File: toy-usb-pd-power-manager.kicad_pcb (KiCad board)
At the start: 4 copper layers, 26.2 x 52.1 mm, 162 parts, among them J1 USB_C_2_0, J2 PINS_LHS, J3 PINS_RHS, Q1 Si7223DN, Q2 Si7224DN, Q3 Si7224DN, Q4 Si7224DN, Q5 Si7223DN, Q6 BSS138PS, Q7 BSS138PS, Q8 BSS138PS, U1 HUSB238_002DD, U2 BQ25672, U3 MAX17205G, U4 TPS63070, U5 TPS7A2601DRVR

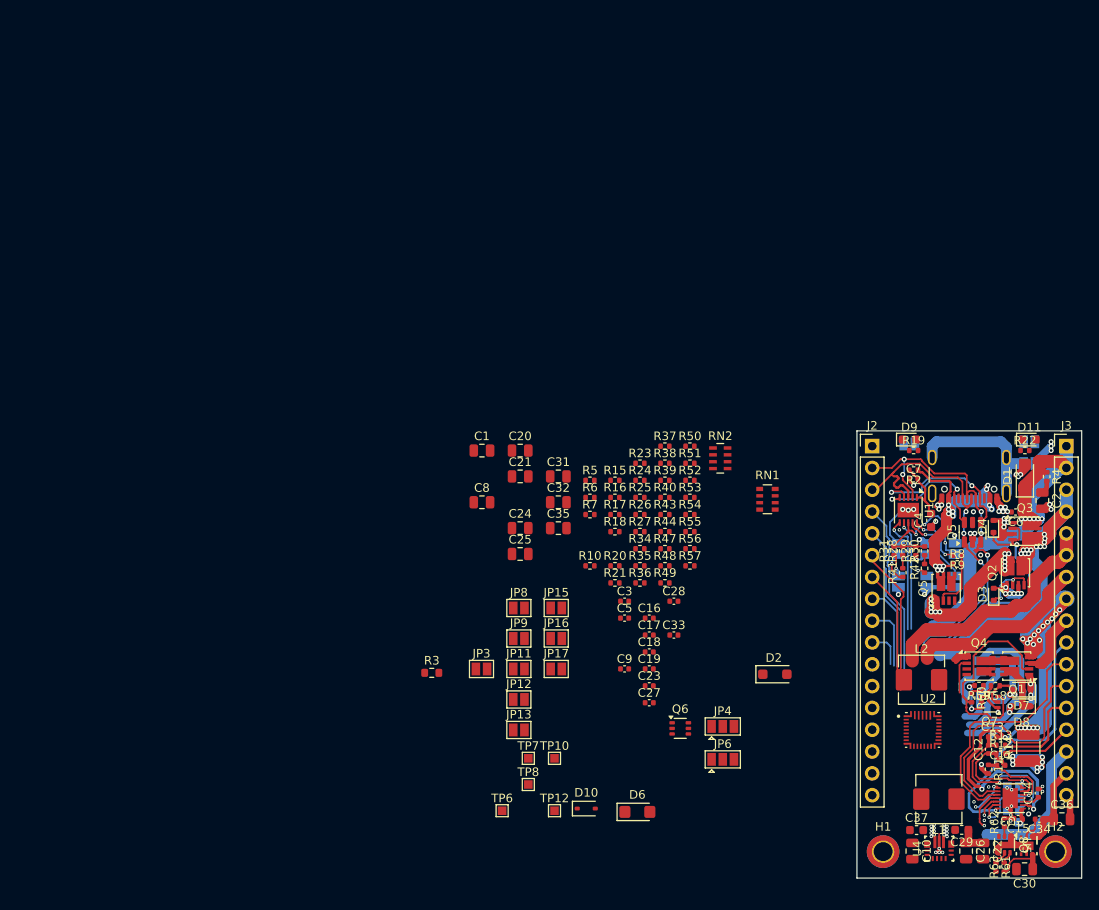
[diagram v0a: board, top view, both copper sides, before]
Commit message: refactor(pcb): improve positioning of ICs on the board
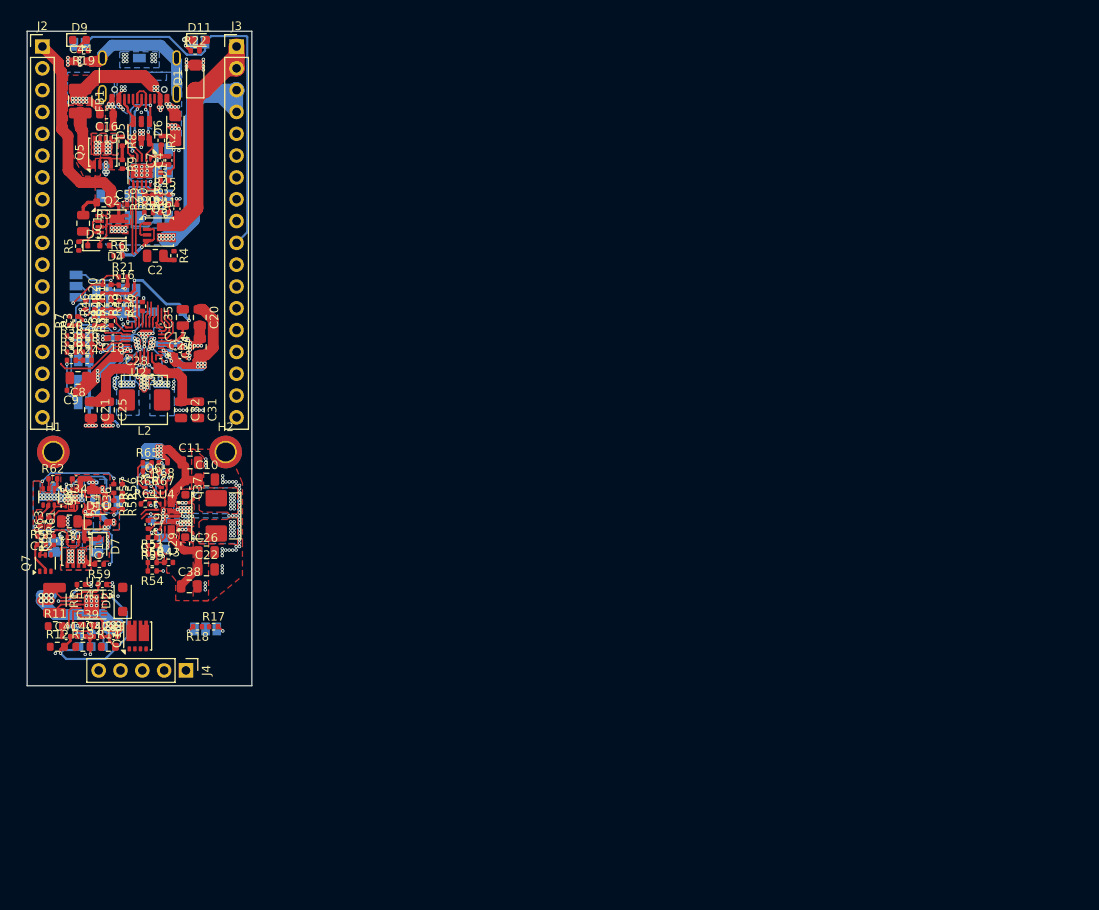
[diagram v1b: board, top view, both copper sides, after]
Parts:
- removed D8: 1N5819WS, Diode_SMD:D_SOD-323
- removed Q4: Si7224DN, Package_SO:Vishay_PowerPAK_1212-8_Dual
- removed RN1: 10M, Resistor_SMD:R_Array_Convex_4x0603
- removed RN2: 1M, Resistor_SMD:R_Array_Concave_4x0603
- removed TP1, TP2, TP3, TP4, TP5: TestPoint, TestPoint:TestPoint_Pad_1.0x1.0mm
- added C38: 47u, Capacitor_SMD:C_0805_2012Metric, F.Cu at (125.5, 119.7)
- added C39: 100n, Capacitor_SMD:C_0402_1005Metric, F.Cu at (113.6, 124.1)
- added C40: 10n, Capacitor_SMD:C_0402_1005Metric, F.Cu at (113.0, 125.5)
- added C41: 10n, Capacitor_SMD:C_0402_1005Metric, F.Cu at (111.1, 125.5)
- added C42: 10n, Capacitor_SMD:C_0402_1005Metric, F.Cu at (114.8, 125.5)
- added C43: 10n, Capacitor_SMD:C_0402_1005Metric, F.Cu at (116.6, 125.5)
- added C44: DNP, Capacitor_SMD:C_0603_1608Metric, F.Cu at (112.8, 58.6)
- added FB1: 8A, Inductor_SMD:L_1210_3225Metric, F.Cu at (112.8, 63.2)
- added J4: PINS_RHS, Connector_PinHeader_2.54mm:PinHeader_1x05_P2.54mm_Vertical, F.Cu at (125.1, 129.5)
- added JP10: BAT_ILIM_2A, Jumper:SolderJumper-2_P1.3mm_Open_Pad1.0x1.5mm, B.Cu at (115.3, 85.2)
- added JP14: BAT_PACK_4S, Jumper:SolderJumper-2_P1.3mm_Open_Pad1.0x1.5mm, B.Cu at (113.2, 98.3)
- added JP24: USB_ISET_2A, Jumper:SolderJumper-2_P1.3mm_Open_Pad1.0x1.5mm, B.Cu at (122.4, 68.9)
- added Q10: DMC3025LDV, mixlib-generic-son:Diodes_PowerDI3333-8_UXC_3.3x3.3mm_P0.65mm, F.Cu at (119.5, 125.5)
- added R1: 0.1, Resistor_SMD:R_1210_3225Metric, F.Cu at (109.8, 121.3)
- added R32: 10K, Resistor_SMD:R_0402_1005Metric, F.Cu at (122.6, 72.4)
- added R33: 1M, Resistor_SMD:R_0402_1005Metric, F.Cu at (115.4, 86.9)
- added R45: 510, Resistor_SMD:R_0402_1005Metric, F.Cu at (122.6, 71.5)
- added R46: 68K, Resistor_SMD:R_0402_1005Metric, F.Cu at (114.5, 86.9)
- added R64: 10M, Resistor_SMD:R_0402_1005Metric, F.Cu at (120.3, 110.1)
- added R65: 10M, Resistor_SMD:R_0402_1005Metric, F.Cu at (120.6, 105.3)
- added R66: 10M, Resistor_SMD:R_0402_1005Metric, F.Cu at (120.6, 106.3)
- added R67: 10M, Resistor_SMD:R_0402_1005Metric, F.Cu at (122.4, 106.3)
- added R68: 10M, Resistor_SMD:R_0402_1005Metric, F.Cu at (122.4, 105.3)
- added TP13: TestPoint, TestPoint:TestPoint_Pad_1.0x1.0mm, B.Cu at (114.1, 125.3)
- added TP14: TestPoint, TestPoint:TestPoint_Pad_1.0x1.0mm, B.Cu at (112.6, 125.3)
- added TP15: TestPoint, TestPoint:TestPoint_Pad_1.0x1.0mm, B.Cu at (115.5, 126.7)
- C11: value 1n -> 22u; footprint Capacitor_SMD:C_0402_1005Metric -> Capacitor_SMD:C_0805_2012Metric
- C12: value 1n -> 100n
- C13: value 1n -> 1u
- C14: value 470n -> 1u
- C15: value 470n -> 2.2u; footprint Capacitor_SMD:C_0402_1005Metric -> Capacitor_SMD:C_0603_1608Metric
- C16: value 100n -> 2.2u; footprint Capacitor_SMD:C_0402_1005Metric -> Capacitor_SMD:C_0603_1608Metric
- C4: value 2.2u -> 1u; footprint Capacitor_SMD:C_0603_1608Metric -> Capacitor_SMD:C_0402_1005Metric
- D3, D4: value Zener_16V -> 16V
- J2, J3: footprint Connector_PinHeader_2.54mm:PinHeader_1x17_P2.54mm_Vertical -> Connector_PinHeader_2.54mm:PinHeader_1x18_P2.54mm_Vertical
- JP11, JP12, JP13, JP15, JP16, JP17, JP3, JP4, JP6, JP8, JP9, TP10, TP12, TP6, TP7, TP8: moved to B.Cu
- R11, R12, R13: footprint Resistor_SMD:R_0402_1005Metric -> Resistor_SMD:R_0603_1608Metric
- R14: value 0.01 -> 100; footprint Resistor_SMD:R_1210_3225Metric -> Resistor_SMD:R_0603_1608Metric
- R63: value 1M -> 10M
- U3: value MAX17205G -> MAX172x5G
- moved C15 133.2 mm to (115.8, 66.2)
- moved C34 118.9 mm to (112.3, 107.2)
- moved C36 118.9 mm to (114.2, 109.5), turned to -90 degrees
- moved Q8 118.4 mm to (109.1, 109.3)
- moved C30 118.3 mm to (111.5, 112.1)
- moved U5 118.3 mm to (111.8, 109.4)
- moved R61 118.3 mm to (108.2, 112.2)
- moved R63 118.3 mm to (109.1, 112.2)
- moved R62 117.8 mm to (109.6, 107.2), turned to 0 degrees
- moved JP25 114.1 mm to (119.7, 57.6), turned to -90 degrees
- moved C14 114.1 mm to (112.9, 119.5), turned to 180 degrees
- moved C12 113.0 mm to (108.3, 113.9), turned to 180 degrees
- moved Q2 112.8 mm to (116.5, 77.5), turned to 0 degrees
- moved D3 112.4 mm to (114.3, 80.0), turned to 0 degrees
- moved R58 112.3 mm to (108.3, 114.8), turned to 0 degrees
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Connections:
- net /BC_SW_SW2 renamed /BC_SW_BTST2
- net Net-(Q6A-D) renamed /VSW_PS_EN_D
- net Net-(Q6B-D) renamed /VSW_EN_D
- C11 pad 1: /FG_VIN -> /VSW_VIN
- C11 pad 2: /FG_CELL2_TP -> GND
- C12 pad 1: /FG_CELL2_TP -> /VLDO_VIN
- C12 pad 2: /FG_CELL1_TP -> GND
- C13 pad 1: /FG_CELL1_TP -> GND
- C13 pad 2: /VBATN -> /FG_REG3
- C14 pad 1: /FG_REG2 -> GND
- C14 pad 2: GND -> /FG_REG2
- C15 pad 1: /FG_REG3 -> GND
- C15 pad 2: GND -> /USB_VBUS
- C16 pad 1: /FG_VIN -> GND
- C16 pad 2: GND -> /USB_VBUS_PRE
- C20 pad 1: /VIN -> /BC_VIN
- C24 pad 1: /VIN -> /BC_VIN
- C27 pad 1: /VIN -> /BC_VIN
- D6 pad 1: /USB_VBUS -> /USB_VBUS_PRE
- J1 pad A4: /USB_VBUS -> /USB_VBUS_PRE
- J1 pad A9: /USB_VBUS -> /USB_VBUS_PRE
- J1 pad B4: /USB_VBUS -> /USB_VBUS_PRE
- J1 pad B9: /USB_VBUS -> /USB_VBUS_PRE
- J2 pad 11: /VSW_VIN -> /FG_TS_VCC
- J2 pad 12: /VLDO_VIN1 -> /FG_TS1
- J2 pad 13: /VLDO_VIN2 -> /FG_TS2
- J2 pad 14: /~{INT} -> GND
- J2 pad 15: /SCL -> /~{INT}
- J2 pad 16: /SDA -> /SCL
- J2 pad 17: GND -> /SDA
- J3 pad 10: /FG_TS_VCC -> /VBATP
- J3 pad 11: /FG_TS2 -> /BC_REGN
- J3 pad 12: /FG_TS1 -> /BC_TS
- J3 pad 13: /FG_CELL1 -> /VSW_VIN
- J3 pad 14: /FG_CELL2 -> /VLDO_VIN1
- J3 pad 15: /VSW -> /VLDO_VIN2
- J3 pad 16: /VLDO -> /VSW
- J3 pad 17: GND -> /VLDO
- J3 pad 8: /VBATN -> /VSYS
- J3 pad 9: /VBATP -> /VBATN
- JP6 pad 2: /FG_TS1 -> /BC_TS
- Q1 pad 3: /VBATP -> /VLDO_VIN2
- Q1 pad 4: /VBATN -> /VLDO_VIN2_EN_S
- Q1 pad 5: /VBATP_RPP -> /VLDO_VIN2_EN_G
- Q1 pad 6: /VLDO_VIN2_S -> /VLDO_VIN2_EN_G
- Q5 pad 1: /VBUS -> /USB_VBUS
- Q5 pad 2: Net-(Q5A-G) -> /USB_VBUS_G
- Q5 pad 3: unconnected-(Q5B-D-Pad3) -> /VBUS
- Q5 pad 4: unconnected-(Q5B-G-Pad4) -> /USB_VBUS_G
- Q5 pad 5: unconnected-(Q5B-S-Pad5) -> /USB_VBUS_D
- Q5 pad 6: /USB_VBUS -> /USB_VBUS_D
- R11 pad 1: /FG_VIN -> /BC_VBAT
- R11 pad 2: /BC_VBAT -> /FG_VCC
- R12 pad 1: /FG_CELL2_TP -> /FG_CELLX
- R12 pad 2: /FG_CELL2 -> /FG_CELLX_IN
- R13 pad 1: /FG_CELL1_TP -> /FG_CELL2
- R13 pad 2: /FG_CELL1 -> /FG_CELL2_IN
- R14 pad 1: GND -> /FG_CELL1
- R14 pad 2: /VBATN -> /FG_CELL1_IN
- R2 pad 1: /USB_VBUS -> /USB_VBUS_PRE
- R59 pad 1: /VLDO_VIN2_S -> /VLDO_VIN2
- R60 pad 1: /VLDO_VIN2_S -> /VLDO_VIN2_EN_G
- R8 pad 1: /USB_VBUS -> /USB_VBUS_D
- R8 pad 2: Net-(Q5A-G) -> /USB_VBUS_G
- R9 pad 1: Net-(Q5A-G) -> /USB_VBUS_G
- TP11 pad 1: /FG_REG3 -> /FG_CELL2_IN
- TP9 pad 1: GND -> /FG_CELLX_IN
- U2 pad 16: /FG_TS1 -> /BC_TS
- U3 pad 13: /FG_CELLX_TP -> /FG_CELLX_IN
- U3 pad 5: /FG_VIN -> /FG_VCC
- U3 pad 6: /FG_CELL2_TP -> /FG_CELL2_IN
- U3 pad 7: /FG_CELL1_TP -> /FG_CELL1_IN
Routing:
- net GND: track 89.4 -> 173.0 mm, vias 56 -> 256
- net /BC_REGN: track 0.00 -> 68.9 mm, vias 0 -> 2
- net /VBATN: track 92.6 -> 27.9 mm, vias 21 -> 12
- net /USB_VBUS: track 44.0 -> 6.44 mm, vias 14 -> 0
- net /BC_VBAT: track 5.38 -> 40.9 mm, vias 1 -> 8
- net /BC_SW_L2: track 0.00 -> 32.7 mm, vias 0 -> 21
- net /USB_D+: track 46.1 -> 14.5 mm, vias 5 -> 2
- net /USB_D-: track 44.5 -> 14.0 mm, vias 3 -> 2
- net /FG_TS_VCC: track 29.7 -> 0.00 mm, vias 1 -> 0
- net /BC_SW_L1: track 0.00 -> 29.7 mm, vias 0 -> 21
- net /FG_TS1: track 28.8 -> 0.00 mm
- net /FG_TS2: track 28.5 -> 0.00 mm
- net /USB_VBUS_PRE: track 0.00 -> 26.4 mm, vias 0 -> 30
- net /BC_VIN: track 43.9 -> 67.8 mm, vias 12 -> 32
- net /VSW_VIN: track 0.00 -> 23.0 mm, vias 0 -> 8
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- added copper zone on B.Cu, net /BC_SW_L1
- added copper zone on B.Cu, net /BC_SW_L2
- added copper zone on B.Cu, net /BC_VIN
- added copper zone on F.Cu, net /USB_VBUS
- added copper zone on B.Cu, net /USB_VBUS_D
- added copper zone on F.Cu, net /USB_VBUS_D
- added copper zone on B.Cu, net /USB_VBUS_PRE
- added copper zone on F.Cu, net /USB_VBUS_PRE
- added copper zone on F.Cu, net /VBUS
- added copper zone on B.Cu, net /VLDO
- added copper zone on F.Cu, net /VLDO
- added copper zone on F.Cu, net /VLDO_VIN
- added copper zone on B.Cu, net /VLDO_VIN1
- added copper zone on F.Cu, net /VLDO_VIN1
- added copper zone on B.Cu, net /VLDO_VIN2
- added copper zone on B.Cu, net /VLDO_VIN2_EN_G
- added copper zone on F.Cu, net /VLDO_VIN2_EN_G
- added copper zone on F.Cu, net /VSW
- added copper zone on B.Cu, net /VSW_SW_L1
- added copper zone on F.Cu, net /VSW_SW_L1
- added copper zone on B.Cu, net /VSW_SW_L2
- added copper zone on F.Cu, net /VSW_SW_L2
- added copper zone on F.Cu, net /VSW_VIN
- added copper zone on B.Cu, net GND
- added copper zone on F.Cu, net GND
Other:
- board size 26.2 x 52.1 mm -> 26.2 x 76.2 mm
